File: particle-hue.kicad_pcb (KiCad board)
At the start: 2 copper layers, 31 parts, among them P1 MOTION_SENSOR, P2 TEMP_SENSOR, SW1 SW_PUSH, SW2 SW_PUSH, SW3 SW_PUSH, SW4 SW_PUSH, SW5 SW_PUSH, SW6 SW_PUSH, U1 PHOTON

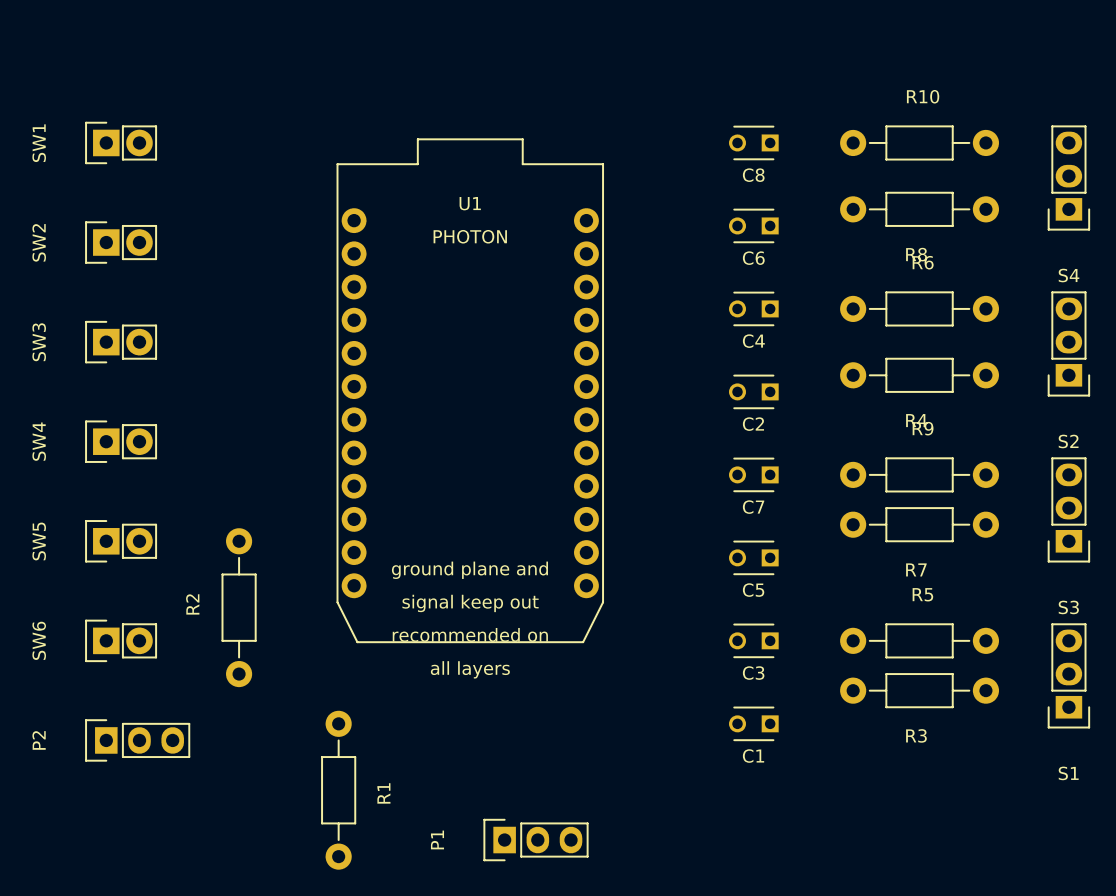
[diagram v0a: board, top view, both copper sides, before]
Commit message: updated to reflect some changes to the software
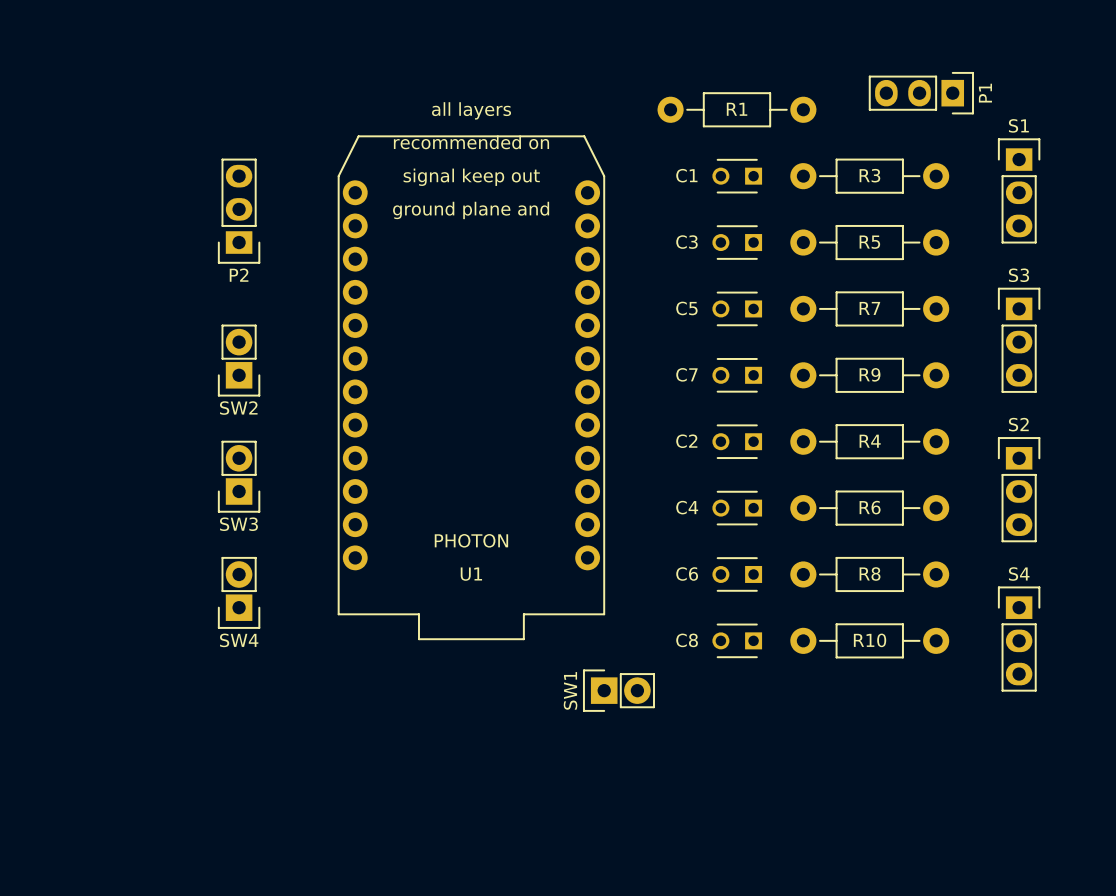
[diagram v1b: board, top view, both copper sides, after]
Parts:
- removed R2: R, Resistors_ThroughHole:Resistor_Horizontal_RM10mm
- removed SW5, SW6: SW_PUSH, Pin_Headers:Pin_Header_Straight_1x02
- C1, C2, C3, C4, C5, C6, C7, C8: value C -> 0.1uF
- R1, R10, R3, R4, R5, R6, R7, R8, R9: value R -> 10k
- moved P1 66.6 mm to (185.4, 80.0), turned to 270 degrees
- moved R1 60.3 mm to (168.9, 81.3), turned to 0 degrees
- moved SW1 56.6 mm to (158.8, 125.7)
- moved S1 42.1 mm to (190.5, 85.1), turned to 0 degrees
- moved C1 41.9 mm to (170.2, 86.4)
- moved R3 39.6 mm to (179.1, 86.4)
- moved P2 39.4 mm to (130.8, 91.4), turned to 180 degrees
- moved R10 38.3 mm to (179.1, 121.9)
- moved C8 38.1 mm to (170.2, 121.9)
- moved R5 30.7 mm to (179.1, 91.4)
- moved S4 30.7 mm to (190.5, 119.4), turned to 0 degrees
- moved C3 30.5 mm to (170.2, 91.4)
- moved R8 28.2 mm to (179.1, 116.8)
- moved C6 26.7 mm to (170.2, 116.8)
- moved C5 19.1 mm to (170.2, 96.5)
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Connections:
- C1 pad 1: /D0 -> /D1
- C2 pad 1: /D4 -> /D3
- C3 pad 1: /D1 -> /A0
- C4 pad 1: /D5 -> /A3
- C6 pad 1: /D6 -> /D4
- C7 pad 1: /D3 -> /A1
- C8 pad 1: /D7 -> /A4
- P1 pad 3: /A0 -> /A2
- P2 pad 2: Net-(P2-Pad2) -> /A5
- R1 pad 1: /A1 -> /A2
- R1 pad 2: GND -> +5V
- R10 pad 1: /D7 -> /A4
- R3 pad 2: /D0 -> /D1
- R4 pad 2: /D4 -> /D3
- R5 pad 1: /D1 -> /A0
- R6 pad 1: /D5 -> /A3
- R8 pad 2: /D6 -> /D4
- R9 pad 1: /D3 -> /A1
- SW2 pad 1: +3V3 -> GND
- SW2 pad 2: Net-(SW2-Pad2) -> /D5
- SW3 pad 1: +3V3 -> GND
- SW3 pad 2: Net-(SW3-Pad2) -> /D6
- SW4 pad 1: +3V3 -> GND
- SW4 pad 2: Net-(SW4-Pad2) -> /D7
- U1 pad 10: Net-(SW6-Pad2) -> /A2
- U1 pad 13: /D0 -> Net-(U1-Pad13)
- U1 pad 6: Net-(SW2-Pad2) -> Net-(U1-Pad6)
- U1 pad 7: Net-(SW3-Pad2) -> /A5
- U1 pad 8: Net-(SW4-Pad2) -> /A4
- U1 pad 9: Net-(SW5-Pad2) -> /A3
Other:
- net class Default: trace_width 0.1524 -> 0.25; via_dia 0.6858 -> 0.6; via_drill 0.3302 -> 0.4
- rule pad_to_mask_clearance: 0.2 -> 0
- rule trace_min: 0.1524 -> 0.2
- rule via_min_drill: 0.3302 -> 0.3
- rule via_min_size: 0.6858 -> 0.4

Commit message: added the traces
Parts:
- added R2: 10k, Resistors_ThroughHole:Resistor_Horizontal_RM10mm, F.Cu at (156.2, 123.2)
- moved P2 28.0 mm to (132.1, 119.4)
- moved SW1 15.5 mm to (143.5, 123.2)
- moved SW2 12.7 mm to (130.8, 88.9)
- moved SW3 12.7 mm to (130.8, 97.8)
- moved SW4 12.7 mm to (130.8, 106.7)
- moved U1 6.35 mm to (148.6, 94.0)
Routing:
- net GND: track 0.00 -> 215.5 mm
- net /D1: track 0.00 -> 73.0 mm
- net /D2: track 0.00 -> 63.7 mm
- net /D3: track 0.00 -> 53.4 mm
- net +5V: track 0.00 -> 51.0 mm
- net /D4: track 0.00 -> 50.0 mm
- net /A4: track 0.00 -> 40.1 mm
- net /A5: track 0.00 -> 35.0 mm
- net /A3: track 0.00 -> 35.0 mm
- net Net-(R2-Pad1): track 0.00 -> 31.8 mm
- net +3V3: track 0.00 -> 28.6 mm
- net /A2: track 0.00 -> 27.6 mm
- net /A1: track 0.00 -> 26.9 mm
- net /A0: track 0.00 -> 24.6 mm
- net /D5: track 0.00 -> 12.8 mm
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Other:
- board outline added: 69.9 x 54.6 mm
- net class Default: trace_width 0.25 -> 0.381; via_dia 0.6 -> 0.6858; via_drill 0.4 -> 0.3302
- rule trace_min: 0.2 -> 0.254
- rule via_min_drill: 0.3 -> 0.3302
- rule via_min_size: 0.4 -> 0.6858
- board text added: "Blockly Hue"
